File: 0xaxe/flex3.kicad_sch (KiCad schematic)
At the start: 97 parts, among them U39 MCP1824T-1802E, U63 25MHz, U65 NCP114ASN080T1G, U66 TLV3544, U67 +0V8_2, U68 +0V8_2, U69 BM1366_mode1, U70 +0V8_2, U71 +0V8_2, U72 +0V8_2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

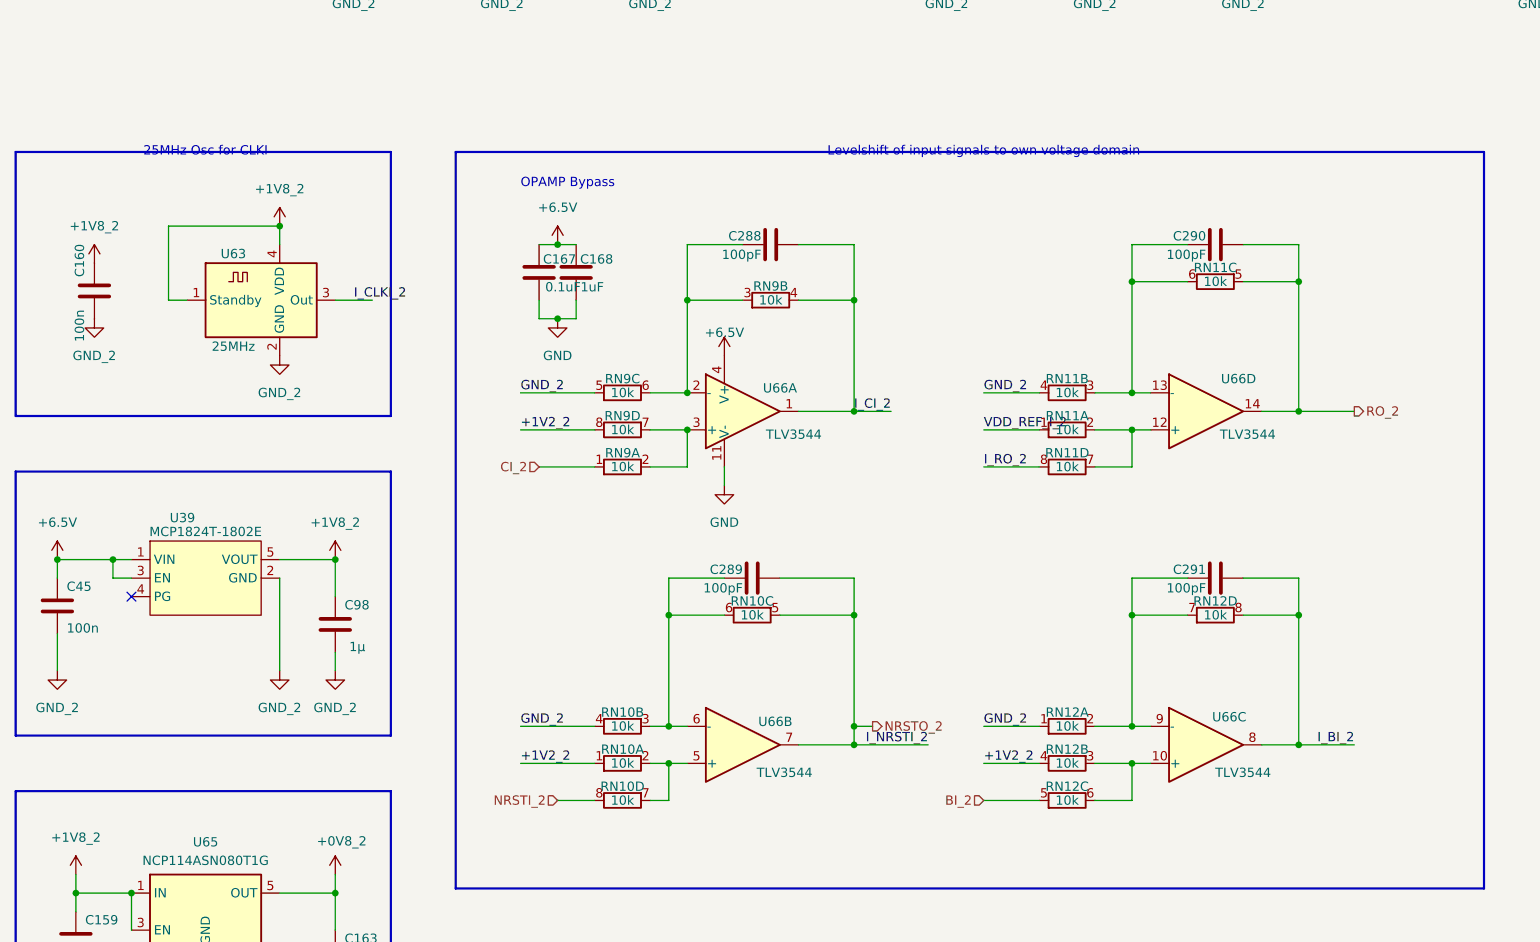
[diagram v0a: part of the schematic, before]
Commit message: fixed level shifter, added optional headers for future extensions
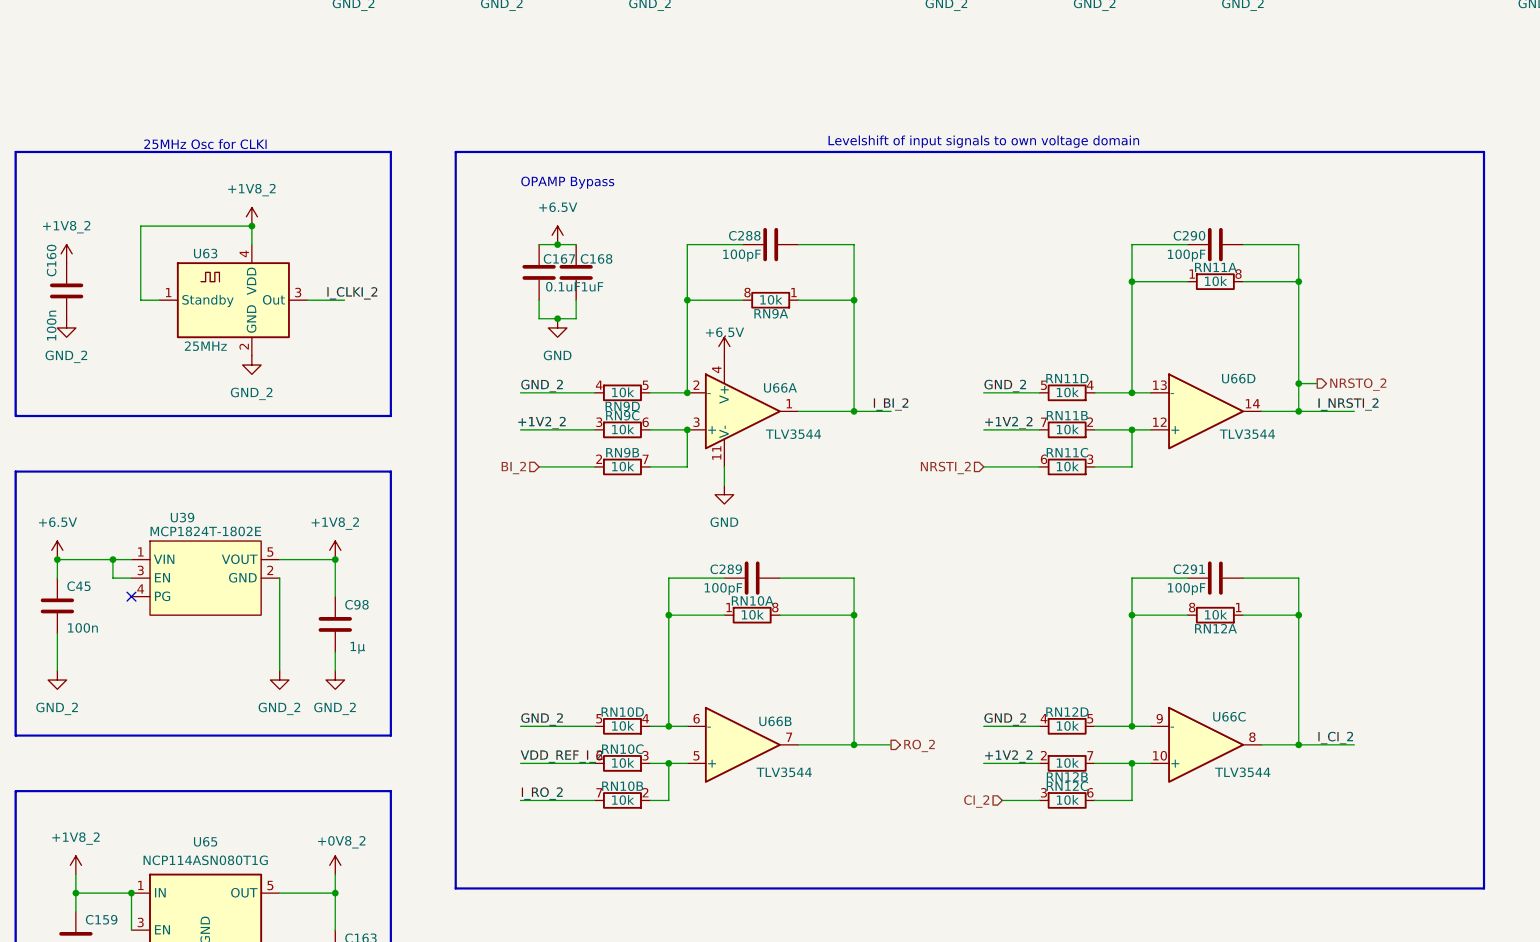
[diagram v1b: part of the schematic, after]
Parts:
- RN10, RN11, RN12, RN9: footprint EXB-28V103JX:EXB28V_PAN -> Resistor_SMD:R_Array_Convex_4x0603; symbol Device:R_Network04_Split -> mylib7:R_Network04_Split_SMD
- U69, U80, U83, U86: footprint bitvein:BM1366 -> myfootprints:BM1366-user1-soldermask
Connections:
- net +1V2_2: now also RN11.7 (R2.2), RN12.2 (R2.1), RN9.3 (R3.1); no longer RN10.1 (R1), RN12.4 (R2.2), RN9.8 (R4.2)
- net BI_2: now also RN9.2 (R2.1); no longer RN12.5 (R2.2)
- net CI_2: now also RN12.3 (R3.1); no longer RN9.1 (R1)
- net GND_2: now also RN10.5 (R4.2), RN11.5 (R4.2), RN12.4 (R4.1), RN9.4 (R4.1); no longer RN10.4 (R2.2), RN11.4 (R2.2), RN12.1 (R1), RN9.5 (R2.2)
- net I_BI_2: now also C288.2, RN9.1 (R1.1), U66.1; no longer C291.2, RN12.8 (R4.2), U66.8
- net I_CI_2: now also C291.2, RN12.1 (R1.1), U66.8; no longer C288.2, RN9.4 (R2.2), U66.1
- net I_RO_2: now also RN10.7 (R2.2); no longer RN11.8 (R4.2)
- net NRSTI_2: now also RN11.6 (R3.2); no longer RN10.8 (R4.2)
- net NRSTO_2: now also C290.2, RN11.8 (R1.2), U66.14; no longer C289.2, RN10.5 (R2.2), U66.7
- net RO_2: now also C289.2, RN10.8 (R1.2), U66.7; no longer C290.2, RN11.5 (R2.2), U66.14
- net VDD_REF_I_2: now also RN10.6 (R3.2); no longer RN11.1 (R1)
- net at C290.1, U66.13 (-): now also RN11.1 (R1.1), RN11.4 (R4.1); no longer RN11.3 (R2.2), RN11.6 (R3.2)
- net at C289.1, U66.6 (-): now also RN10.1 (R1.1), RN10.4 (R4.1); no longer RN10.3 (R2.2), RN10.6 (R3.2)
- net at C291.1, U66.9 (-): now also RN12.5 (R4.2), RN12.8 (R1.2); no longer RN12.2 (R1.2), RN12.7 (R2.2)
- net at RN12.6 (R3.2), U66.10 (+): now also RN12.7 (R2.2); no longer RN12.3 (R2.2)
- net at C288.1, U66.2 (-): now also RN9.5 (R4.2), RN9.8 (R1.2); no longer RN9.3 (R2.2), RN9.6 (R3.2)
- new net: RN11.2 (R2.1), RN11.3 (R3.1), U66.12 (+)
- new net: RN10.2 (R2.1), RN10.3 (R3.1), U66.5 (+)
- new net: RN9.6 (R3.2), RN9.7 (R2.2), U66.3 (+)
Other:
- moved on the sheet: C160, RN10A, RN10B, RN10C, RN10D, RN11A, RN11B, RN11C, RN11D, RN12A, RN12B, RN12D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

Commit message: updated BOM and gerbers
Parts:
- C167: value 0.1uF -> 100n
- C168: value 1uF -> 1µ
- C288, C289, C290, C291: value 100pF -> 100p
- RN10, RN11, RN12, RN9: value 10k -> 10k-CX; Distributor (none) -> D; Manufacturer (none) -> CAY16-1002F4LF; OrderNr (none) -> CAY16-1002F4LFCT-ND
- U66: value TLV3544 -> TLV9154; Distributor (none) -> D; Manufacturer (none) -> TLV9154IDR; OrderNr (none) -> 296-TLV9154IDRCT-ND
